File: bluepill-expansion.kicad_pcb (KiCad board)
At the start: 2 copper layers, 12 parts, among them J1 SENSE_A, J2 SENSE_B, J3 POWER_DC, J4 MOTDC1, J5 MOTDC2, J6 I2C, J7 UART, J8 CAN_BUS, U1 BluePill_STM32F103C, U2 L298HN

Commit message: first routing
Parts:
- added C1: 0.1uF, Capacitor_THT:C_Disc_D7.5mm_W2.5mm_P5.00mm, F.Cu at (161.5, 113.8)
- added C2: 100nF, Capacitor_THT:C_Disc_D7.5mm_W2.5mm_P5.00mm, F.Cu at (141.5, 74.2)
- added C3: 100nF, Capacitor_THT:C_Disc_D7.5mm_W2.5mm_P5.00mm, F.Cu at (113.8, 66.3)
- added C4: 0.1uF, Capacitor_THT:C_Disc_D7.5mm_W2.5mm_P5.00mm, F.Cu at (141.7, 113.8)
- added D1: D_Schottky, Diode_THT:D_DO-41_SOD81_P12.70mm_Horizontal, F.Cu at (167.9, 96.5)
- added D2: D_Schottky, Diode_THT:D_DO-41_SOD81_P12.70mm_Horizontal, F.Cu at (180.6, 93.0)
- added D3: D_Schottky, Diode_THT:D_DO-41_SOD81_P12.70mm_Horizontal, F.Cu at (167.9, 85.9)
- added D4: D_Schottky, Diode_THT:D_DO-41_SOD81_P12.70mm_Horizontal, F.Cu at (180.6, 89.4)
- added D5: D_Schottky, Diode_THT:D_DO-41_SOD81_P12.70mm_Horizontal, F.Cu at (167.9, 78.7)
- added D6: D_Schottky, Diode_THT:D_DO-41_SOD81_P12.70mm_Horizontal, F.Cu at (180.6, 82.3)
- added D7: D_Schottky, Diode_THT:D_DO-41_SOD81_P12.70mm_Horizontal, F.Cu at (167.9, 71.6)
- added D8: D_Schottky, Diode_THT:D_DO-41_SOD81_P12.70mm_Horizontal, F.Cu at (180.6, 75.2)
- added J10: ENCODERS, TerminalBlock:TerminalBlock_bornier-6_P5.08mm, F.Cu at (140.2, 59.9)
- added J11: LS2, Connector_PinHeader_2.54mm:PinHeader_1x02_P2.54mm_Vertical, F.Cu at (145.5, 110.0)
- added J12: I/O 3V3, Connector_PinSocket_2.54mm:PinSocket_1x09_P2.54mm_Vertical, F.Cu at (109.7, 84.3)
- added J13: DIGITAL_PWR, Connector_PinHeader_2.54mm:PinHeader_1x02_P2.54mm_Vertical, F.Cu at (105.4, 59.9)
- added J9: LS1, Connector_PinHeader_2.54mm:PinHeader_1x02_P2.54mm_Vertical, F.Cu at (165.4, 110.0)
- added R1: R, Resistor_THT:R_Box_L26.0mm_W5.0mm_P20.00mm, F.Cu at (176.3, 101.3)
- added R2: R, Resistor_THT:R_Box_L26.0mm_W5.0mm_P20.00mm, F.Cu at (176.3, 66.3)
- added R3: 10k, Resistor_THT:R_Axial_DIN0207_L6.3mm_D2.5mm_P10.16mm_Horizontal, F.Cu at (166.9, 118.4)
- added R4: 10k, Resistor_THT:R_Axial_DIN0207_L6.3mm_D2.5mm_P10.16mm_Horizontal, F.Cu at (147.1, 118.4)
- added SW1: LS1, Button_Switch_THT:SW_PUSH_6mm_H8.5mm, F.Cu at (177.0, 113.8)
- added SW2: LS2, Button_Switch_THT:SW_PUSH_6mm_H8.5mm, F.Cu at (157.2, 114.0)
- C6: value 100uF -> 10uF
- moved J2 32.2 mm to (150.9, 67.6), turned to 180 degrees
- moved J1 30.3 mm to (150.4, 100.1), turned to 0 degrees
- moved C5 26.2 mm to (187.5, 101.1), turned to 180 degrees
- moved J7 24.6 mm to (109.7, 79.2)
- moved J3 22.8 mm to (184.9, 111.0), turned to 90 degrees
- moved U2 21.3 mm to (160.3, 96.5)
- moved C6 21.3 mm to (184.9, 115.8), turned to 270 degrees
- moved J8 20.0 mm to (145.8, 102.1), turned to 180 degrees
- moved U1 18.9 mm to (120.0, 69.2)
- moved J6 18.3 mm to (109.7, 117.3)
- moved J4 11.7 mm to (186.4, 92.7)
- moved J5 7.52 mm to (186.4, 80.5)
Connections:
- U1 pad 1: (no net) -> VCC
- U1 pad 10: (no net) -> /PA5
- U1 pad 11: (no net) -> /PA6
- U1 pad 12: (no net) -> /PA7
- U1 pad 13: (no net) -> /PB0
- U1 pad 14: (no net) -> /PB1
- U1 pad 21: (no net) -> LS1
- U1 pad 22: (no net) -> LS2
- U1 pad 23: (no net) -> ENB
- U1 pad 24: (no net) -> ENA
- U1 pad 27: CANTX -> (no net)
- U1 pad 29: (no net) -> CANTX
- U1 pad 30: (no net) -> ENC1_D
- U1 pad 31: ENA -> ENC1_Q
- U1 pad 32: ENB -> (no net)
- U1 pad 33: (no net) -> /PB5
- U1 pad 34: (no net) -> ENC2_D
- U1 pad 35: (no net) -> ENC2_Q
- U1 pad 5: (no net) -> /PA0
- U1 pad 6: (no net) -> /PA1
- U1 pad 9: (no net) -> /PA4
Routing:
- net +3V3: track 93.9 -> 0.00 mm
- net GND: track 47.4 -> 128.0 mm
- net LS1: track 0.00 -> 70.1 mm
- net VCC: track 11.2 -> 77.2 mm
- net ENC1_D: track 0.00 -> 42.2 mm
- net MOT3: track 7.52 -> 47.0 mm
- net ENC1_Q: track 0.00 -> 37.5 mm
- net MOT2: track 6.51 -> 41.5 mm
- net LS2: track 0.00 -> 32.8 mm
- net ENC2_D: track 0.00 -> 29.1 mm
- net ENC2_Q: track 0.00 -> 26.5 mm
- net +5V: track 92.1 -> 68.7 mm
- net ENA: track 22.3 -> 0.00 mm
- net PWM1: track 58.5 -> 39.0 mm
- net MOT4: track 26.4 -> 45.5 mm
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
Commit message: routing update
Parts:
- moved J13 5.59 mm to (109.7, 63.5), turned to 180 degrees
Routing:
- net GND: track 128.0 -> 361.4 mm
- net +3V3: track 0.00 -> 87.8 mm, vias 0 -> 2
- net /PB5: track 0.00 -> 73.8 mm, vias 0 -> 2
- net VCC: track 77.2 -> 144.1 mm
- net +5V: track 68.7 -> 123.5 mm, vias 0 -> 1
- net UARTTX: track 0.64 -> 22.0 mm, vias 0 -> 2
- net UARTRX: track 0.00 -> 20.4 mm, vias 0 -> 2
- net ENC2_D: track 29.1 -> 27.7 mm
- net ENC2_Q: track 26.5 -> 25.5 mm
- net /PA1: track 12.3 -> 13.1 mm

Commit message: final routing sin revisar
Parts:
- moved U2 10.1 mm to (158.2, 86.6)
- moved D7 6.35 mm to (167.9, 65.3)
- moved D8 6.35 mm to (180.6, 68.8)
- moved R2 6.35 mm to (176.3, 59.9)
- moved J2 6.10 mm to (150.9, 61.5)
- moved D6 4.32 mm to (180.6, 78.0)
- moved D5 4.32 mm to (167.9, 74.4)
- moved J8 4.13 mm to (142.7, 99.3)
- moved J1 2.59 mm to (150.9, 102.6), turned to 180 degrees
- moved D3 2.29 mm to (167.9, 83.6)
- moved D4 2.29 mm to (180.6, 87.1)
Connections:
- U1 pad 24: ENA -> (no net)
- U1 pad 32: (no net) -> ENA
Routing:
- net GND: track 361.4 -> 473.1 mm, vias 0 -> 2
- net +5V: track 123.5 -> 214.0 mm, vias 1 -> 2
- net ENB: track 0.00 -> 61.8 mm
- net VCC: track 144.1 -> 176.0 mm
- net ENA: track 0.00 -> 21.7 mm
- net MOT3: track 47.0 -> 34.4 mm
- net SENSE_A: track 13.4 -> 22.7 mm
- net MOT2: track 41.5 -> 34.8 mm
- net PWM2: track 45.5 -> 51.7 mm
- net SENSE_B: track 20.0 -> 15.7 mm
- net PWM3: track 22.4 -> 19.6 mm
- net PWM4: track 22.4 -> 19.6 mm
- net CANTX: track 10.6 -> 8.71 mm
- net CANRX: track 10.6 -> 8.75 mm
- net MOT4: track 45.5 -> 47.0 mm
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
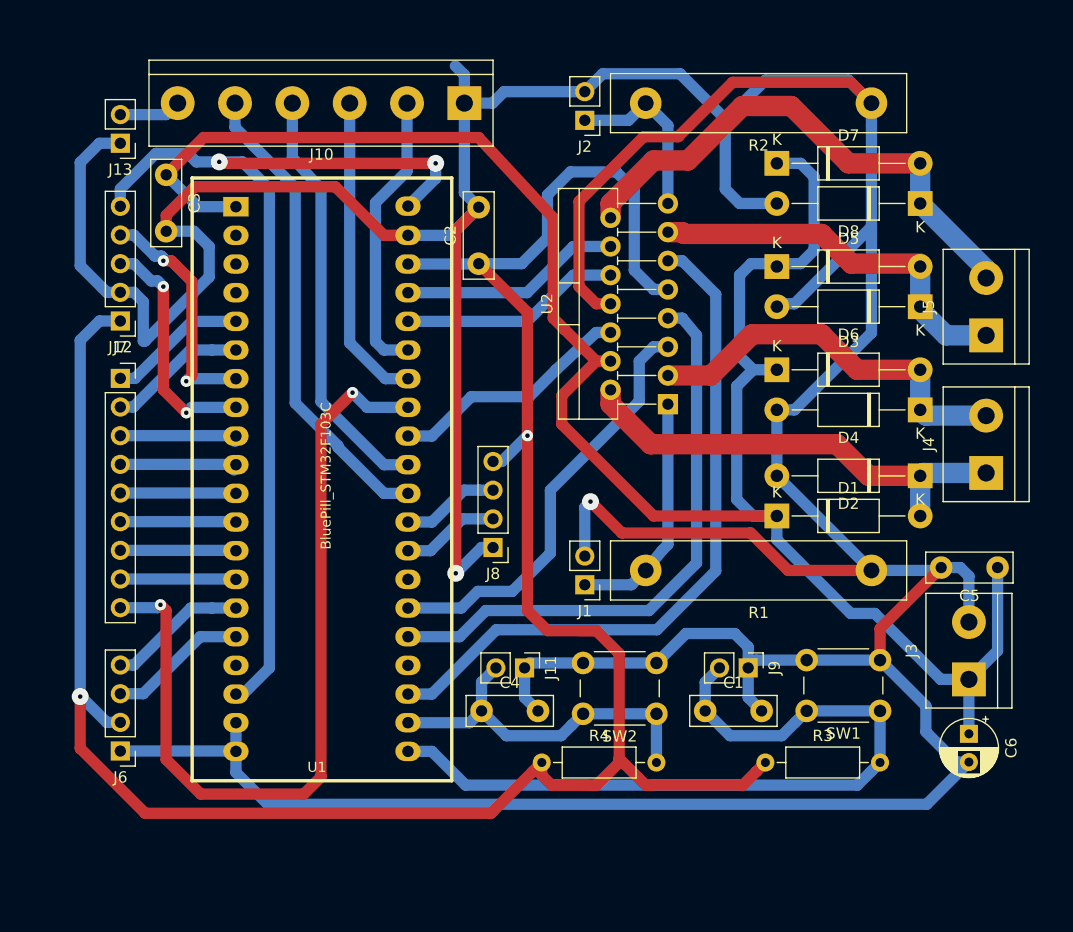
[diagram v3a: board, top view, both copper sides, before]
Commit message: added edge cuts and GND
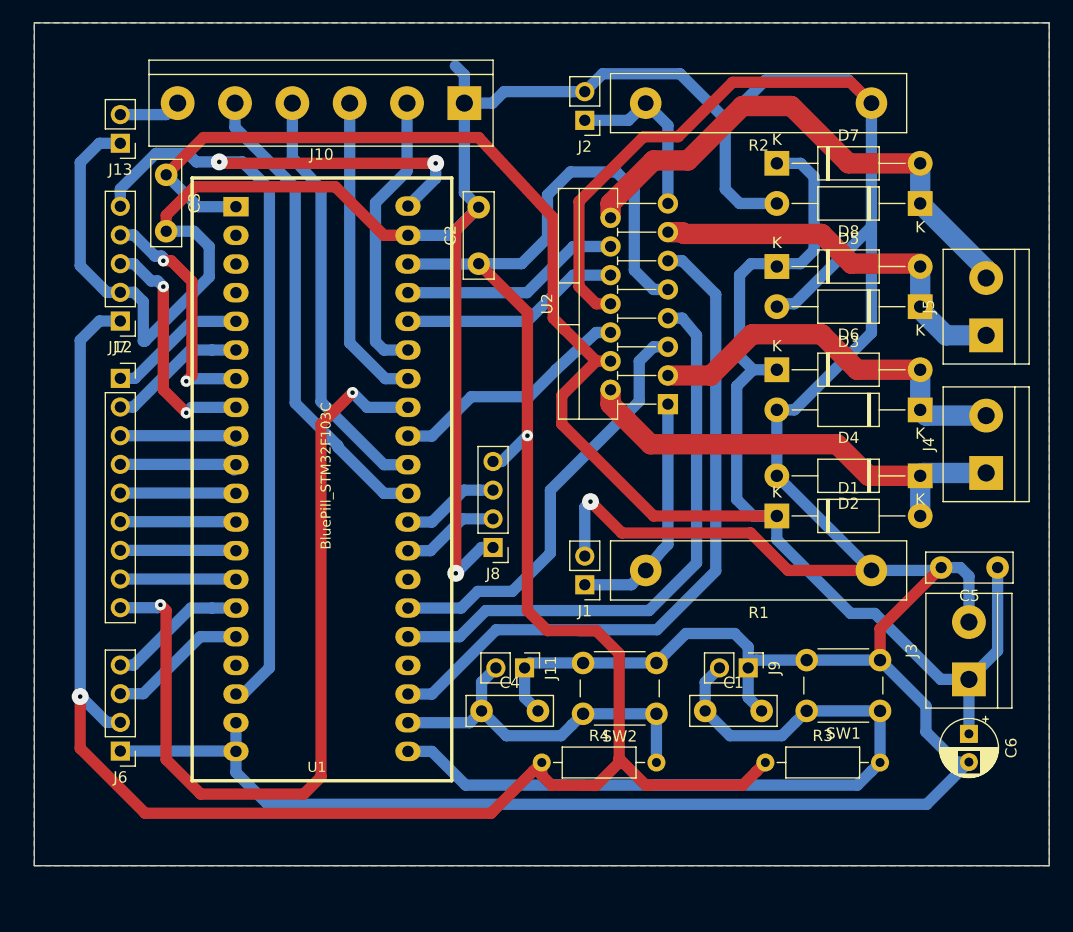
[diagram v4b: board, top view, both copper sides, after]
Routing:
- added copper zone on B.Cu, net GND
- added copper zone on F.Cu, net GND
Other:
- board outline added: 89.9 x 74.7 mm
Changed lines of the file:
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@@
   (general
     (thickness 1.6)
-    (drawings 0)
+    (drawings 4)
     (tracks 403)
     (zones 0)
@@
     )
   )
+  (gr_line (start 192.024 52.832) (end 102.108 52.832) (layer Edge.Cuts) (width 0.05))
+  (gr_line (start 192.024 127.508) (end 192.024 52.832) (layer Edge.Cuts) (width 0.05))
+  (gr_line (start 102.108 127.508) (end 192.024 127.508) (layer Edge.Cuts) (width 0.05))
+  (gr_line (start 102.108 52.832) (end 102.108 127.508) (layer Edge.Cuts) (width 0.05))
   (via (at 139.446 101.6) (size 1.5) (drill 0.4) (layers F.Cu B.Cu) (net 1))
   (via (at 106.172 112.522) (size 1.5) (drill 0.4) (layers F.Cu B.Cu) (net 3))
@@
   (segment (start 116.065048 79.2786) (end 119.9714 79.2786) (width 1) (layer B.Cu) (net 37))
   (segment (start 111.015648 84.328) (end 116.065048 79.2786) (width 1) (layer B.Cu) (net 37))
+  (zone (net 1) (net_name GND) (layer B.Cu) (hatch edge 0.508)
+    (connect_pads (clearance 0.508))
+    (min_thickness 0.254)
+    (fill yes (arc_segments 32) (thermal_gap 0.508) (thermal_bridge_width 0.508))
+    (polygon
+      (pts
+        (xy 192.024 127.508) (xy 102.108 127.508) (xy 102.108 52.832) (xy 192.024 52.832)
+      )
+    )
+  )
+  (zone (net 1) (net_name GND) (layer F.Cu) (hatch edge 0.508)
+    (connect_pads (clearance 0.508))
+    (min_thickness 0.254)
+    (fill yes (arc_segments 32) (thermal_gap 0.508) (thermal_bridge_width 0.508))
+    (polygon
+      (pts
+        (xy 192.024 127.508) (xy 102.108 127.508) (xy 102.108 52.832) (xy 192.024 52.832)
+      )
+    )
+  )
 )

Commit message: added MCP2551 for CAN
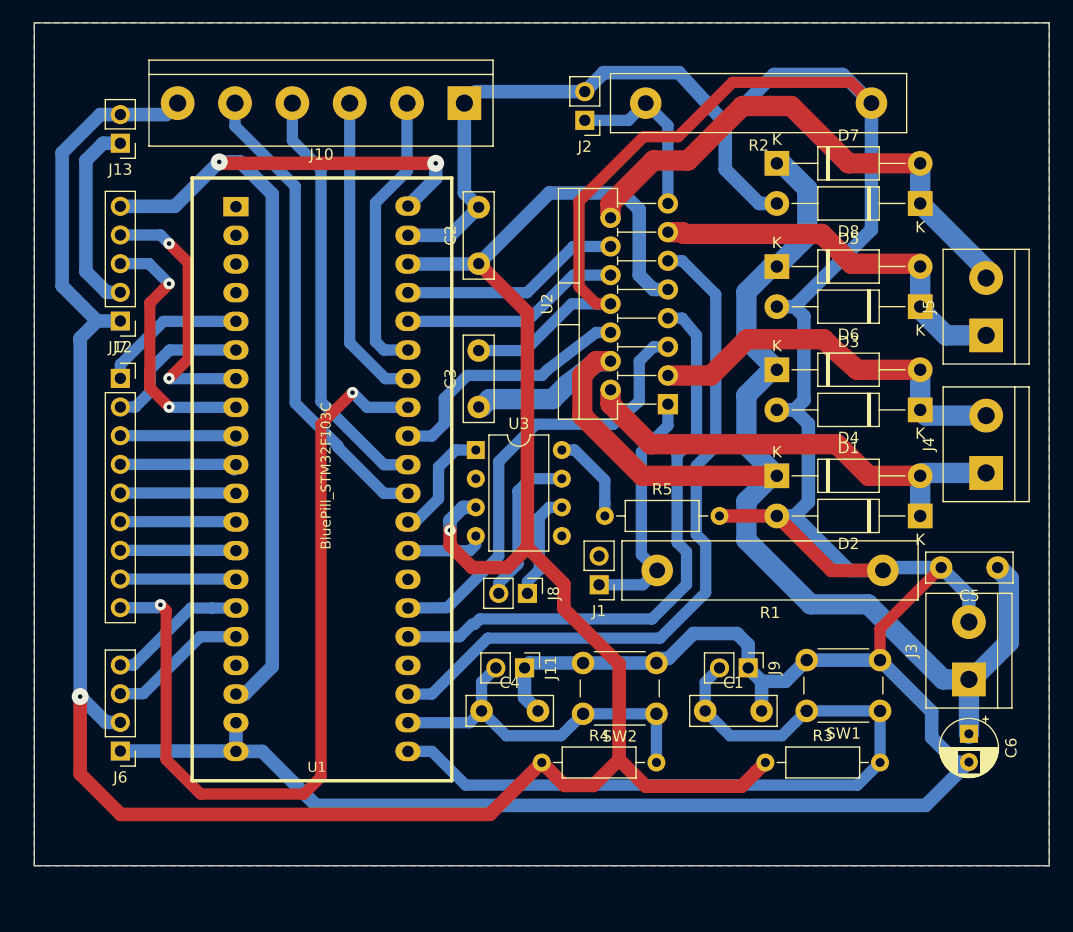
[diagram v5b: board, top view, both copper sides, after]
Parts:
- added R5: 10k, Resistor_THT:R_Axial_DIN0207_L6.3mm_D2.5mm_P10.16mm_Horizontal, F.Cu at (152.7, 96.5)
- added U3: MCP2551-I-P, Package_DIP:DIP-8_W7.62mm, F.Cu at (141.2, 90.7)
- J8: footprint Connector_PinHeader_2.54mm:PinHeader_1x04_P2.54mm_Vertical -> Connector_PinHeader_2.54mm:PinHeader_1x02_P2.54mm_Vertical
- moved C3 34.5 mm to (141.5, 86.9), turned to 90 degrees
- moved J8 5.08 mm to (145.8, 103.4), turned to 270 degrees
- moved D1 3.56 mm to (167.9, 93.0)
- moved D2 3.56 mm to (180.6, 96.5)
- moved J1 1.27 mm to (152.1, 102.6)
- moved R1 1.02 mm to (177.3, 101.3)
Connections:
- J8 pad 1: GND -> /CANL
- J8 pad 2: CANRX -> /CANH
- U1 pad 1: VCC -> (no net)
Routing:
- net GND: track 473.1 -> 374.6 mm, vias 2 -> 0
- net VCC: track 176.0 -> 122.8 mm
- net +5V: track 214.0 -> 238.7 mm
- net /CANH: track 0.00 -> 14.1 mm
- net /CANL: track 0.00 -> 9.55 mm
- net Net-(R5-Pad1): track 0.00 -> 8.08 mm
- net CANRX: track 8.75 -> 6.28 mm
- net UARTTX: track 22.4 -> 24.6 mm
- net UARTRX: track 21.3 -> 23.4 mm
- net CANTX: track 8.71 -> 10.3 mm
- net PWM1: track 38.0 -> 39.5 mm
- net PWM2: track 51.7 -> 53.0 mm
- net ENB: track 61.8 -> 63.1 mm
- net /PA1: track 12.3 -> 13.5 mm
- net ENA: track 21.7 -> 22.8 mm
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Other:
- net class POWER: clearance 0.4 -> 0.5; trace_width 1 -> 1.2

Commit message: fixed line error
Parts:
- moved R5 0.76 mm to (151.9, 96.5)
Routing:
- net PWM2: track 53.0 -> 53.9 mm
- net ENB: track 63.1 -> 63.8 mm
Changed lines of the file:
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@@
   )
   (module Resistor_THT:R_Axial_DIN0207_L6.3mm_D2.5mm_P10.16mm_Horizontal (layer F.Cu)
-    (at 152.654 96.52)
+    (at 151.892 96.52)
     (descr "Resistor, Axial_DIN0207 series, Axial, Horizontal, pin pitch=10.16mm, 0.25W = 1/4W, length*diameter=6.3*2.5mm^2, http://cdn-reichelt.de/documents/datenblatt/B400/1_4W%23YAG.pdf")
     (tags "Resistor Axial_DIN0207 series Axial Horizontal pin pitch 10.16mm 0.25W = 1/4W length 6.3mm diameter 2.5mm")
@@
   (segment (start 165.193999 90.263999) (end 167.894 92.964) (width 1.8) (layer B.Cu) (net 2))
   (segment (start 165.193999 85.825999) (end 165.193999 90.263999) (width 1.8) (layer B.Cu) (net 2))
-  (segment (start 167.453998 92.964) (end 167.894 92.964) (width 1.8) (layer B.Cu) (net 2))
   (segment (start 184.912 110.998) (end 182.626 110.998) (width 1.8) (layer B.Cu) (net 2))
-  (segment (start 165.193999 98.645999) (end 165.193999 95.223999) (width 1.8) (layer B.Cu) (net 2))
-  (segment (start 165.193999 95.223999) (end 167.453998 92.964) (width 1.8) (layer B.Cu) (net 2))
   (segment (start 182.626 110.998) (end 175.974001 104.346001) (width 1.8) (layer B.Cu) (net 2))
   (segment (start 175.974001 104.346001) (end 170.894001 104.346001) (width 1.8) (layer B.Cu) (net 2))
@@
   (segment (start 141.478 86.868) (end 141.732 86.868) (width 1.8) (layer B.Cu) (net 2))
   (segment (start 141.732 86.868) (end 142.431989 86.168011) (width 1.8) (layer B.Cu) (net 2))
+  (segment (start 167.453998 92.964) (end 167.894 92.964) (width 1.8) (layer B.Cu) (net 2))
+  (segment (start 165.193999 95.223999) (end 167.453998 92.964) (width 1.8) (layer B.Cu) (net 2))
+  (segment (start 165.193999 98.645999) (end 165.193999 95.223999) (width 1.8) (layer B.Cu) (net 2))
   (via (at 106.172 112.522) (size 1.5) (drill 0.4) (layers F.Cu B.Cu) (net 3))
   (segment (start 141.4474 74.1986) (end 141.478 74.168) (width 1.2) (layer B.Cu) (net 3))
@@
   (segment (start 146.558 88.392) (end 153.416 88.392) (width 1) (layer B.Cu) (net 17))
   (segment (start 153.416 88.392) (end 155.702 86.36) (width 1) (layer B.Cu) (net 17))
-  (segment (start 159.514792 78.994) (end 158.242 78.994) (width 1) (layer B.Cu) (net 18))
-  (segment (start 160.782 89.408) (end 160.782 80.518) (width 1) (layer B.Cu) (net 18))
-  (segment (start 141.126735 106.104088) (end 141.584834 105.645989) (width 1) (layer B.Cu) (net 18))
-  (segment (start 160.782 80.518) (end 159.514792 78.994) (width 1) (layer B.Cu) (net 18))
-  (segment (start 140.902088 106.104088) (end 141.126735 106.104088) (width 1) (layer B.Cu) (net 18))
   (segment (start 141.584834 105.645989) (end 156.840013 105.645989) (width 1) (layer B.Cu) (net 18))
   (segment (start 135.2114 107.2186) (end 139.787576 107.2186) (width 1) (layer B.Cu) (net 18))
+  (segment (start 141.126735 106.104088) (end 141.584834 105.645989) (width 1) (layer B.Cu) (net 18))
+  (segment (start 159.892001 102.594001) (end 159.892001 99.694001) (width 1) (layer B.Cu) (net 18))
+  (segment (start 140.902088 106.104088) (end 141.126735 106.104088) (width 1) (layer B.Cu) (net 18))
+  (segment (start 159.514792 78.994) (end 158.242 78.994) (width 1) (layer B.Cu) (net 18))
+  (segment (start 157.988 92.202) (end 160.782 89.408) (width 1) (layer B.Cu) (net 18))
   (segment (start 139.787576 107.2186) (end 140.902088 106.104088) (width 1) (layer B.Cu) (net 18))
   (segment (start 156.840013 105.645989) (end 159.892001 102.594001) (width 1) (layer B.Cu) (net 18))
-  (segment (start 159.892001 102.594001) (end 159.892001 99.694001) (width 1) (layer B.Cu) (net 18))
-  (segment (start 159.892001 99.694001) (end 159.056001 98.858001) (width 1) (layer B.Cu) (net 18))
-  (segment (start 159.056001 91.133999) (end 160.782 89.408) (width 1) (layer B.Cu) (net 18))
-  (segment (start 159.056001 98.858001) (end 159.056001 91.133999) (width 1) (layer B.Cu) (net 18))
+  (segment (start 160.782 80.518) (end 159.514792 78.994) (width 1) (layer B.Cu) (net 18))
+  (segment (start 157.988 97.79) (end 157.988 92.202) (width 1) (layer B.Cu) (net 18))
+  (segment (start 159.892001 99.694001) (end 157.988 97.79) (width 1) (layer B.Cu) (net 18))
+  (segment (start 160.782 89.408) (end 160.782 80.518) (width 1) (layer B.Cu) (net 18))
   (segment (start 149.86 75.184) (end 153.162 75.184) (width 1) (layer B.Cu) (net 19))
   (segment (start 135.2114 79.2786) (end 145.7654 79.2786) (width 1) (layer B.Cu) (net 19))
@@
   (segment (start 135.2114 76.7386) (end 145.7654 76.7386) (width 1) (layer B.Cu) (net 20))
   (segment (start 145.7654 76.7386) (end 149.86 72.644) (width 1) (layer B.Cu) (net 20))
+  (segment (start 162.48201 76.881218) (end 159.514792 73.914) (width 1) (layer B.Cu) (net 21))
+  (segment (start 162.482009 90.112167) (end 162.48201 76.881218) (width 1) (layer B.Cu) (net 21))
+  (segment (start 159.825088 97.222912) (end 159.825088 92.769088) (width 1) (layer B.Cu) (net 21))
+  (segment (start 161.592011 98.989834) (end 159.825088 97.222912) (width 1) (layer B.Cu) (net 21))
+  (segment (start 137.3364 112.2986) (end 142.289001 107.345999) (width 1) (layer B.Cu) (net 21))
+  (segment (start 157.544179 107.345999) (end 161.592011 103.298168) (width 1) (layer B.Cu) (net 21))
   (segment (start 159.514792 73.914) (end 158.242 73.914) (width 1) (layer B.Cu) (net 21))
-  (segment (start 162.48201 90.34601) (end 162.48201 76.881218) (width 1) (layer B.Cu) (net 21))
+  (segment (start 159.825088 92.769088) (end 162.482009 90.112167) (width 1) (layer B.Cu) (net 21))
+  (segment (start 161.592011 103.298168) (end 161.592011 98.989834) (width 1) (layer B.Cu) (net 21))
   (segment (start 135.2114 112.2986) (end 137.3364 112.2986) (width 1) (layer B.Cu) (net 21))
-  (segment (start 161.592011 98.989834) (end 160.756011 98.153834) (width 1) (layer B.Cu) (net 21))
-  (segment (start 137.3364 112.2986) (end 142.289001 107.345999) (width 1) (layer B.Cu) (net 21))
   (segment (start 142.289001 107.345999) (end 157.544179 107.345999) (width 1) (layer B.Cu) (net 21))
-  (segment (start 162.48201 76.881218) (end 159.514792 73.914) (width 1) (layer B.Cu) (net 21))
-  (segment (start 160.756011 92.072009) (end 162.48201 90.34601) (width 1) (layer B.Cu) (net 21))
-  (segment (start 160.756011 98.153834) (end 160.756011 92.072009) (width 1) (layer B.Cu) (net 21))
-  (segment (start 161.592011 103.298168) (end 161.592011 98.989834) (width 1) (layer B.Cu) (net 21))
-  (segment (start 157.544179 107.345999) (end 161.592011 103.298168) (width 1) (layer B.Cu) (net 21))
   (segment (start 147.574 83.566) (end 151.889208 80.264) (width 1) (layer B.Cu) (net 22))
   (segment (start 147.071999 84.068001) (end 147.574 83.566) (width 1) (layer B.Cu) (net 22))
@@
   (segment (start 117.8464 79.2786) (end 119.9714 79.2786) (width 1) (layer B.Cu) (net 37))
   (segment (start 109.728 84.328) (end 109.728 83.108002) (width 1) (layer B.Cu) (net 37))
-  (segment (start 152.654 95.38863) (end 152.654 96.52) (width 1) (layer B.Cu) (net 38))
-  (segment (start 152.654 93.35663) (end 152.654 95.38863) (width 1) (layer B.Cu) (net 38))
-  (segment (start 149.97537 90.678) (end 152.654 93.35663) (width 1) (layer B.Cu) (net 38))
+  (segment (start 151.892 95.38863) (end 151.892 96.52) (width 1) (layer B.Cu) (net 38))
+  (segment (start 151.892 92.59463) (end 151.892 95.38863) (width 1) (layer B.Cu) (net 38))
+  (segment (start 149.97537 90.678) (end 151.892 92.59463) (width 1) (layer B.Cu) (net 38))
   (segment (start 148.844 90.678) (end 149.97537 90.678) (width 1) (layer B.Cu) (net 38))
   (segment (start 143.256 102.480176) (end 144.956009 100.780168) (width 1) (layer B.Cu) (net 39))
